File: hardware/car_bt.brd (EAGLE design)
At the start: 100 x 30 mm, 51 parts, among them IC2 MIC5209, U1 ATMEGA328P_TQFP, U2 ADP1710-2.5V, Y1 11.0592MHz

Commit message: selected components
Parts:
- added C21: 22uF, resistor:C1206
- added C22: 22uF, SparkFun-Passives:EIA3528
- C1, C2, C3: value 47uF -> 22uF; device resistor:C1210 -> resistor:C1206
- C11, C12, C13, C15, C16, C17, C18, C19, C20, C7, C8: device resistor:C1210 -> resistor:C0805
- C4, C5: device resistor:C0603 -> resistor:C0805
- L1: value 12uH -> 10uH; device resistor:L3225P -> resistor:L3216C
- R1, R11, R12, R13, R14, R2, R21, R3, R4, R5, R6, R7, R8: device rcl:R0603 -> rcl:R0805
- R10: value 330 -> 360; device rcl:R0603 -> rcl:R0805
- R9: value 470 -> 360; device rcl:R0603 -> rcl:R0805
- moved C1 98.6 mm to (98.0, 73.0), turned to 0 degrees
- moved C2 79.5 mm to (98.0, 66.0), turned to 0 degrees
- moved C3 68.3 mm to (98.0, 59.0), turned to 0 degrees
- moved L1 24.8 mm to (3.00, 27.0)
- moved R9 11.2 mm to (8.00, 27.0), turned to 180 degrees
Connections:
- net +5V: now also C2.1, C22.A; no longer C1.1
- net DGND: now also C1.2, C21.2; no longer C2.2
- net GND: now also C2.2, C22.C; no longer C1.2
- net V+: now also C21.1
- net VCC-ISO: now also C1.1; no longer C2.1

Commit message: v 1.0 of hardware completed
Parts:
- JP2: value (none) -> CAR_IN; device pinhead:1X08 -> pinhead:1X08/90
- Q2: value (none) -> 2N3904
- moved C3 95.6 mm to (9.00, 24.2)
- moved R9 90.4 mm to (98.4, 28.2), turned to 270 degrees
- moved U2 84.0 mm to (86.8, 37.8)
- moved C9 83.0 mm to (91.4, 36.6), turned to 0 degrees
- moved C21 78.0 mm to (49.2, 19.2), turned to 90 degrees
- moved R10 76.7 mm to (82.8, 20.2), turned to 270 degrees
- moved C2 74.5 mm to (32.2, 31.0)
- moved C1 74.3 mm to (42.8, 23.2), turned to 270 degrees
- moved JP5 71.3 mm to (4.50, 18.3)
- moved C14 66.6 mm to (81.8, 37.8)
- moved C22 63.7 mm to (32.0, 34.0), turned to 180 degrees
- moved C5 62.2 mm to (53.6, 19.6), turned to 90 degrees
- moved C10 59.6 mm to (35.6, 15.0), turned to 270 degrees
- moved C4 58.1 mm to (45.0, 22.8), turned to 270 degrees
- moved C19 58.1 mm to (97.4, 24.2), turned to 180 degrees
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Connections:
- net V+: no longer R5.1
- net VCC-ISO: now also R5.1
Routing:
- net GND: track 0.00 -> 195.5 mm, vias 0 -> 3
- net +5V: track 0.00 -> 176.5 mm, vias 0 -> 2
- net DGND: track 0.00 -> 143.5 mm
- net V+: track 0.00 -> 95.3 mm
- net VCC-ISO: track 0.00 -> 94.1 mm
- net RX: track 0.00 -> 85.2 mm, vias 0 -> 1
- net TX: track 0.00 -> 84.9 mm, vias 0 -> 1
- net CRST: track 0.00 -> 41.7 mm
- net OUT_RESET: track 0.00 -> 41.1 mm
- net MOSI: track 0.00 -> 38.9 mm
- net VCCIO: track 0.00 -> 38.3 mm
- net MISO: track 0.00 -> 31.5 mm
- net AGND: track 0.00 -> 24.6 mm
- net CRQ: track 0.00 -> 23.4 mm, vias 0 -> 2
- net N$12: track 0.00 -> 22.0 mm
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- added copper zone on layer 1, net DGND
- added copper zone on layer 1, net GND
- added copper zone on layer 16, net GND
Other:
- board size 100 x 30 mm -> 99.8 x 46 mm
- board text added: "+5V"
- board text added: "AGND"
- board text added: "BLAUPUNKT Gamma V Z1Z3 tape emulator. v1.0. By Dmitry Shagin."
- board text added: "GND"
- board text added: "L"
- board text added: "MIC"
- board text added: "MISO"
- board text added: "MOSI"
- board text added: "R"
- board text added: "RESET"
- board text added: "SCK"
- board text added: "XS3868"

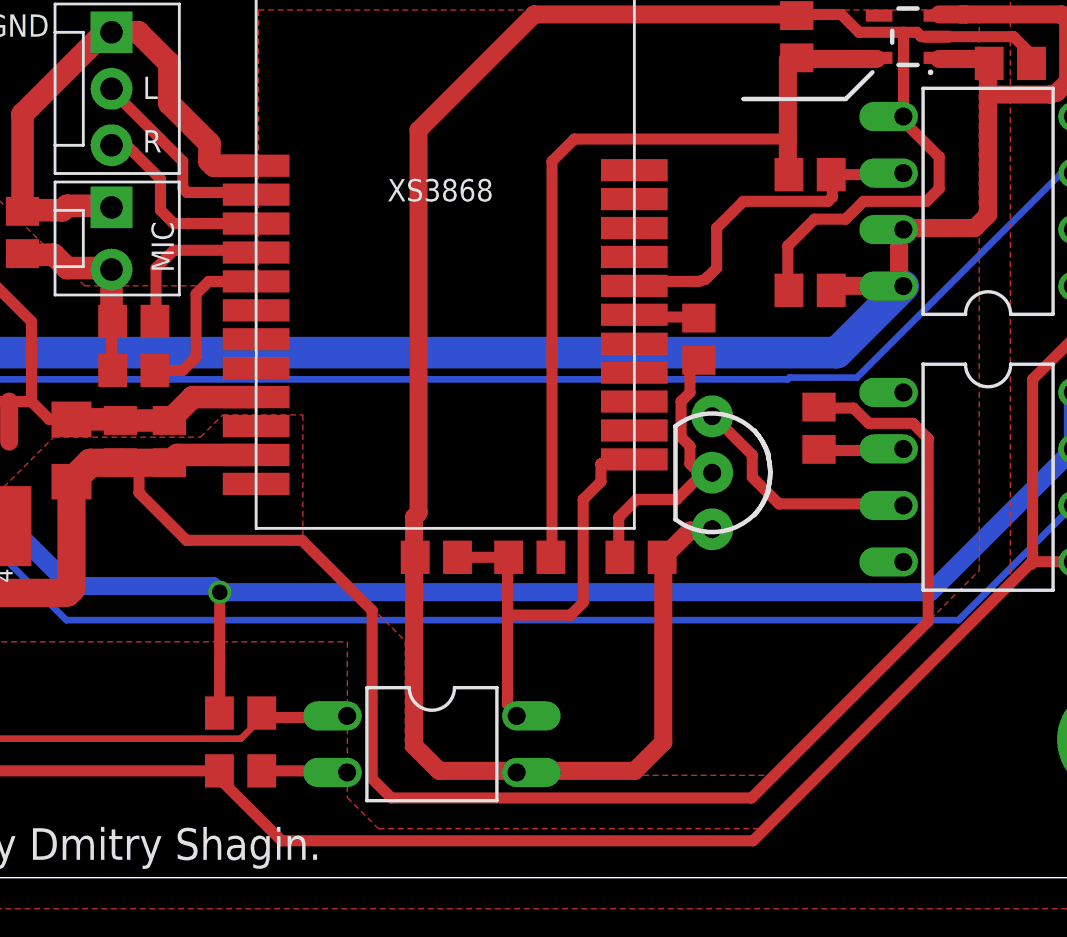
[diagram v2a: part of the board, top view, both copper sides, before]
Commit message: switched to uart
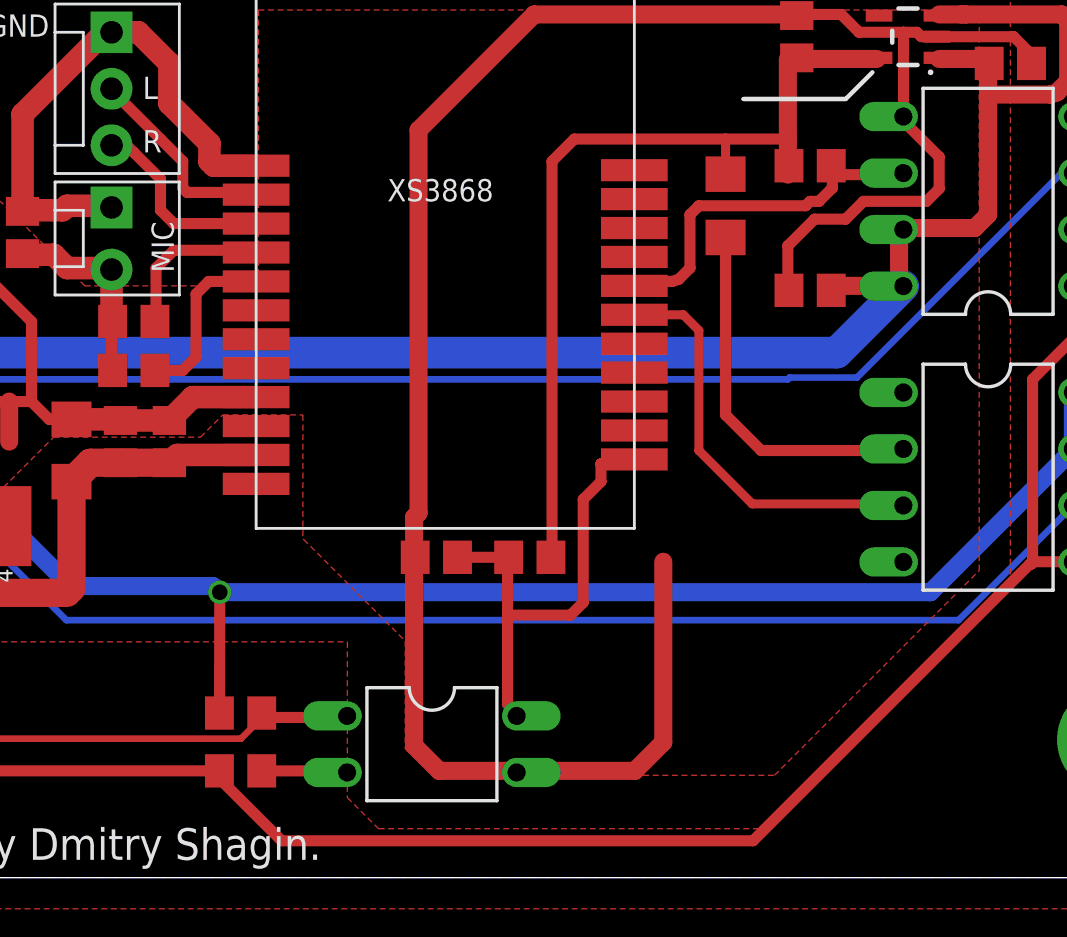
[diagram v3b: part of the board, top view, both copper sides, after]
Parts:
- removed Q2: 2N3904, SparkFun-DiscreteSemi:TO-92-AMMO
- removed R12: 470, rcl:R0805
- removed R13: 10k, rcl:R0805
- R10: value 360 -> 220; device rcl:R0805 -> rcl:R1206
- R21: value 10k -> 360k
- moved R10 10.8 mm to (78.6, 30.2)
- moved R8 0.40 mm to (82.4, 32.0)
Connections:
- removed net N$17: Q2.2, R12.2, R13.2
- removed net N$21: OK6.3, Q2.1
- net DGND: no longer Q2.3, R13.1
- net GND: now also JP2.8
- net N$5: now also OK6.3; no longer R12.1
- net V+: no longer R10.1
- net VCCIO: now also R10.1
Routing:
- net V+: track 95.3 -> 31.6 mm
- net N$5: track 3.07 -> 18.8 mm
- net N$17: track 13.4 -> 0.00 mm
- net N$15: track 3.85 -> 16.6 mm
- net N$21: track 10.9 -> 0.00 mm
- net DGND: track 143.5 -> 140.5 mm
- net VCCIO: track 38.3 -> 40.2 mm
- net N$14: track 15.8 -> 16.6 mm
